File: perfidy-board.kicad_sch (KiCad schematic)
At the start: 572 parts

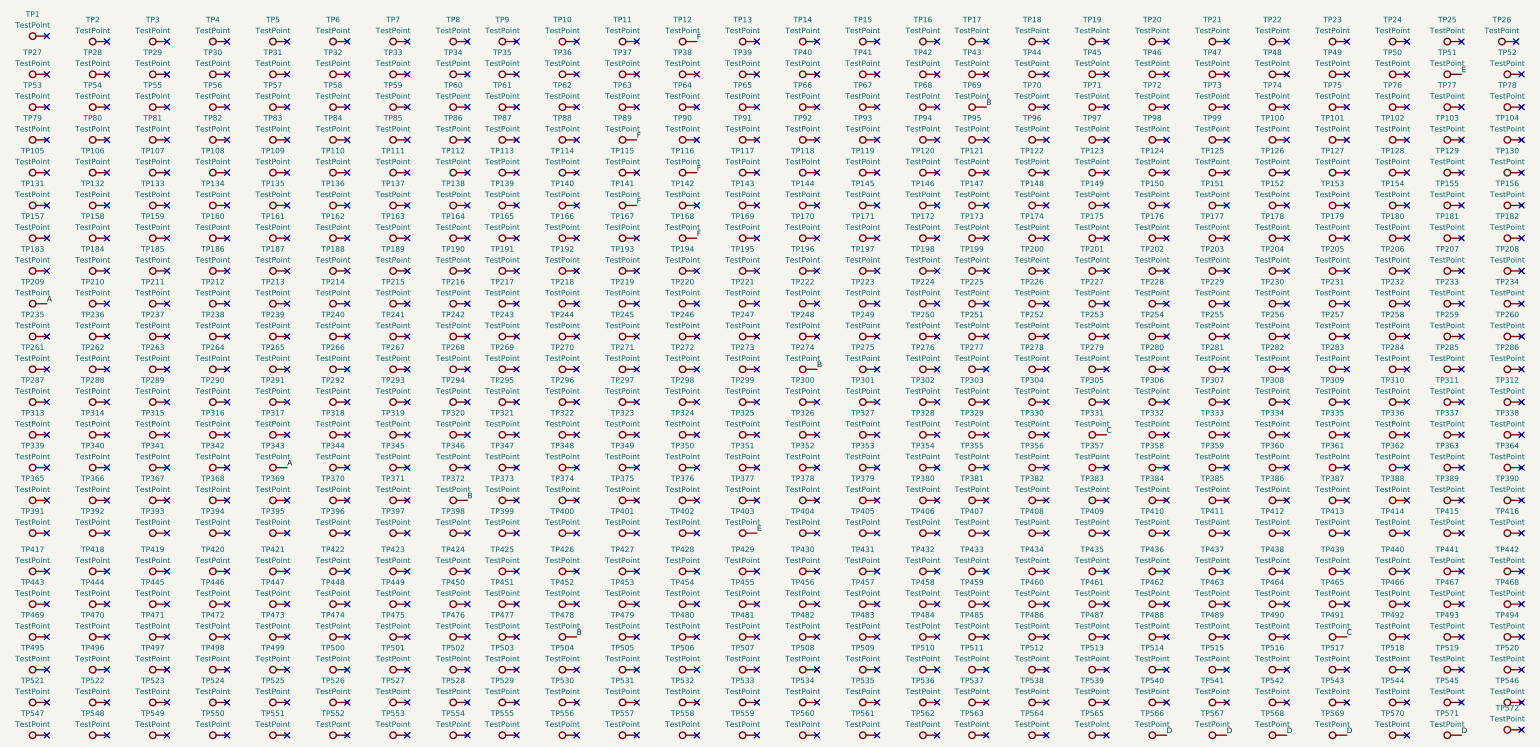
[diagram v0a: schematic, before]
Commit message: v1.1 changes mid layers to hidden text
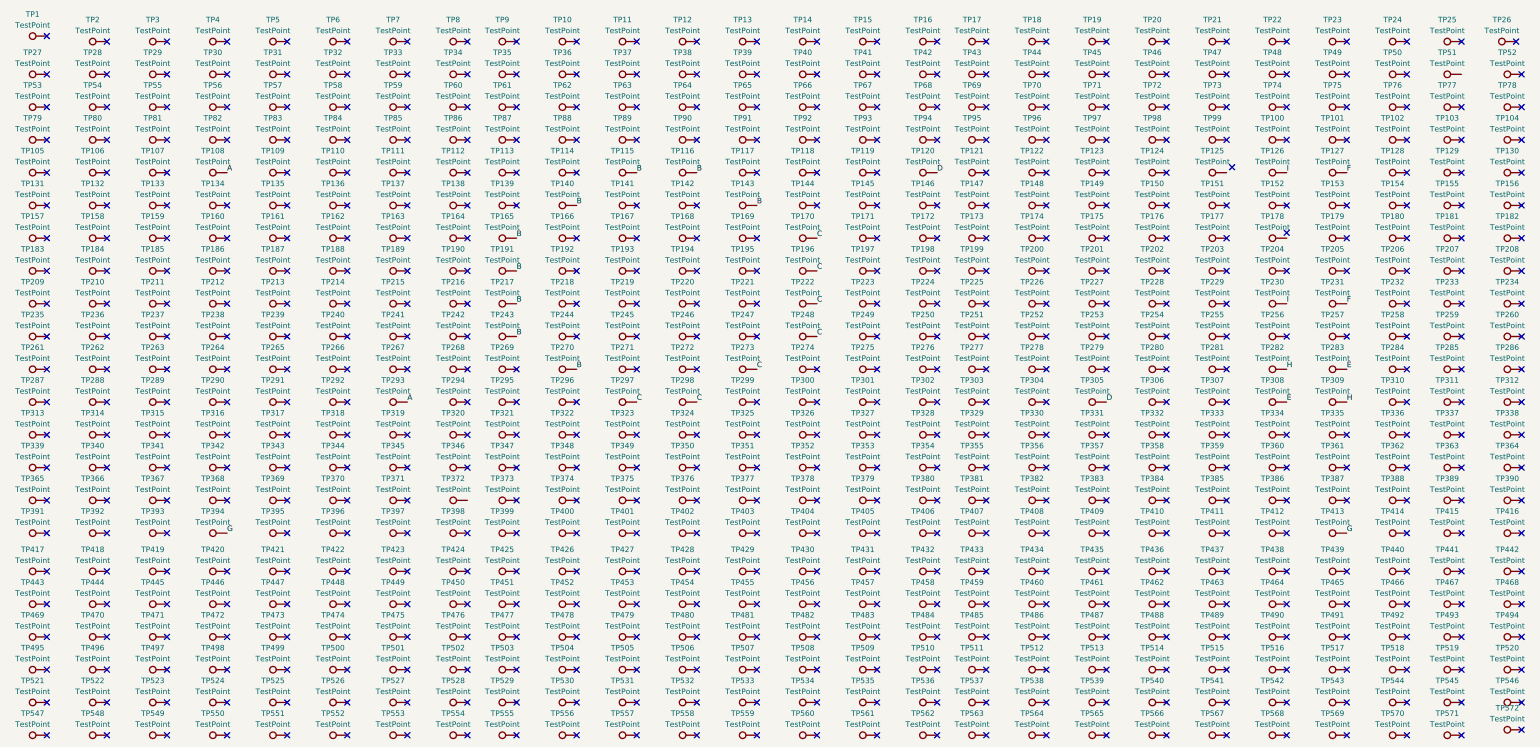
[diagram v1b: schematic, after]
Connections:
- net A: now also TP108.1, TP293.1; no longer TP209.1, TP343.1
- net B: now also TP115.1, TP116.1, TP140.1, TP143.1, TP165.1, TP191.1, TP217.1, TP243.1, TP270.1; no longer TP274.1, TP372.1, TP478.1, TP69.1
- net C: now also TP170.1, TP196.1, TP222.1, TP248.1, TP273.1, TP297.1, TP298.1; no longer TP331.1, TP491.1
- net D: now also TP120.1, TP305.1; no longer TP566.1, TP567.1, TP568.1, TP569.1, TP571.1
- net E: now also TP283.1, TP308.1; no longer TP403.1, TP51.1
- net F: now also TP127.1, TP231.1; no longer TP116.1, TP12.1, TP141.1, TP168.1, TP89.1
- net I: now reaches TP230.1
- net I: now also TP126.1
- net G: now reaches TP413.1
- net G: now also TP394.1
- net H: now reaches TP309.1
- net H: now also TP282.1
- no-connect marks 552 -> 540
